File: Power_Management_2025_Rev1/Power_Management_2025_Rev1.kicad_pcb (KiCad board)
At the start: 2 copper layers, 213.1 x 179.3 mm, 100 parts, among them J1 RJ45_LED_Shielded, Q1 BSS138, Q2 IPB180N10S4-02, Q3 IPB180N10S4-02, Q4 IPB180N10S4-02, U1 Teensy4.1_DEV-16771, U10 LT1910, U11 LT1910, U12 PKE3316ZPI, U13 PKE3316ZPI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

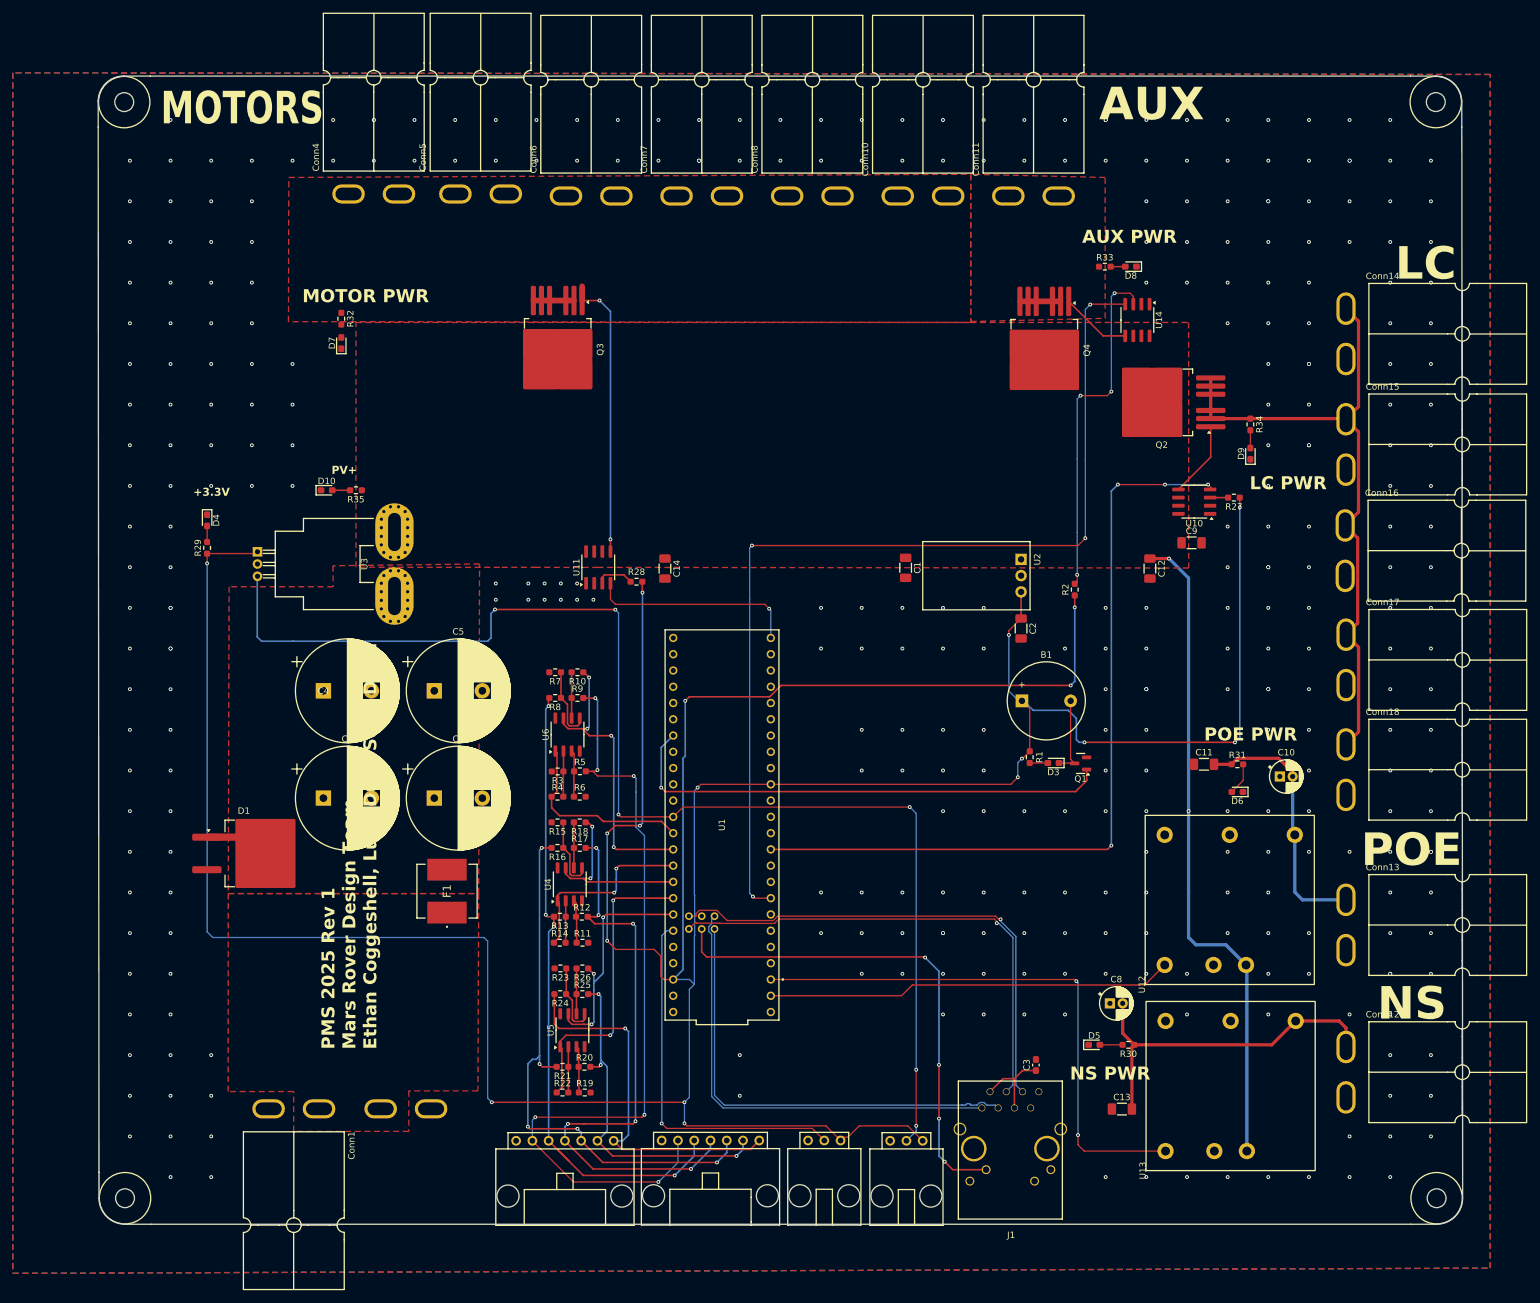
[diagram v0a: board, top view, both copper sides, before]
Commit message: Power plane, diff pair, and mil width fix`
Fixed Motor power plane, readjusted diff pair, and fixed mil width
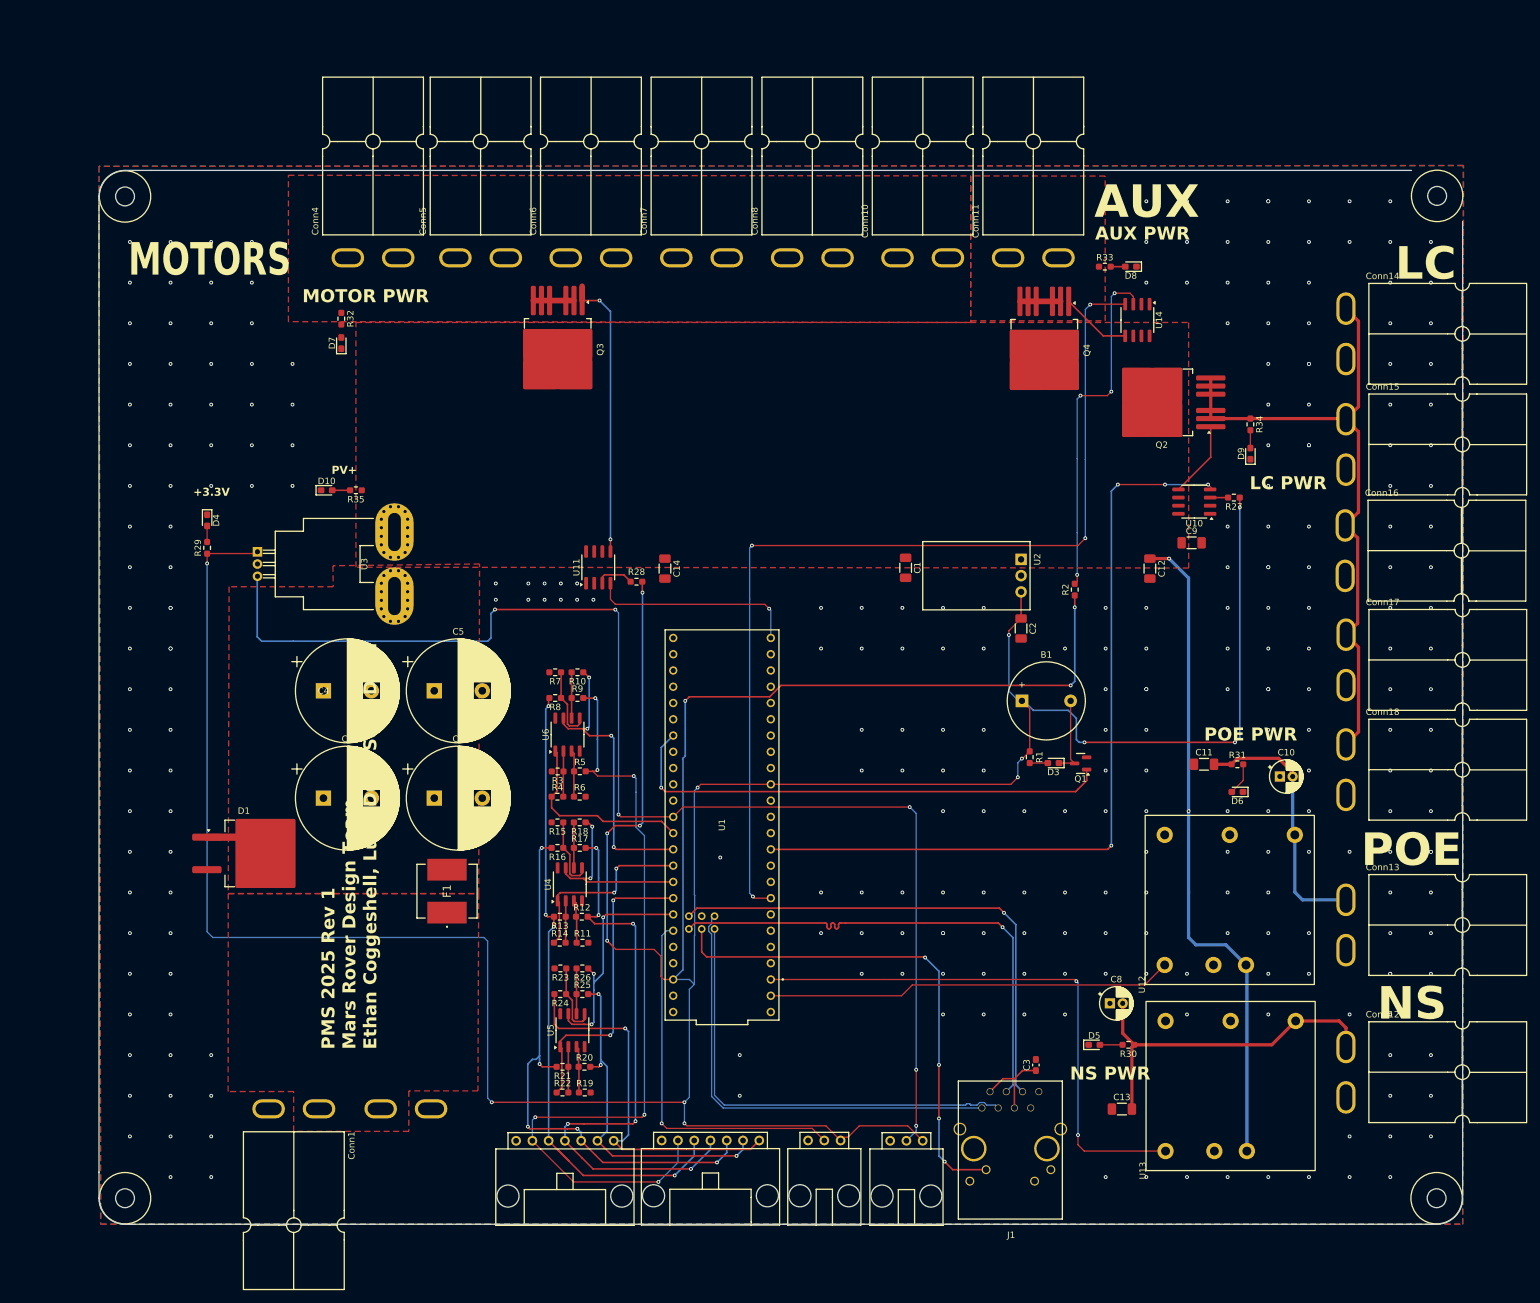
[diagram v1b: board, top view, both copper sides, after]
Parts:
- moved H3 14.7 mm to (35.0, 35.0)
- moved H1 14.7 mm to (231.9, 34.9)
- moved Conn4 9.97 mm to (74.0, 40.7)
- moved Conn5 9.97 mm to (90.8, 40.7)
- moved Conn11 9.65 mm to (177.1, 40.7)
- moved Conn6 9.65 mm to (108.0, 40.7)
- moved Conn7 9.65 mm to (125.3, 40.7)
- moved Conn8 9.65 mm to (142.6, 40.7)
- moved Conn10 9.65 mm to (159.8, 40.7)
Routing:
- net RX+: track 77.3 -> 79.1 mm
- net GND: vias 353 -> 282
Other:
- board size 213.1 x 179.3 mm -> 213 x 164.6 mm

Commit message: Fixed diff pair and rearranged Cap bank
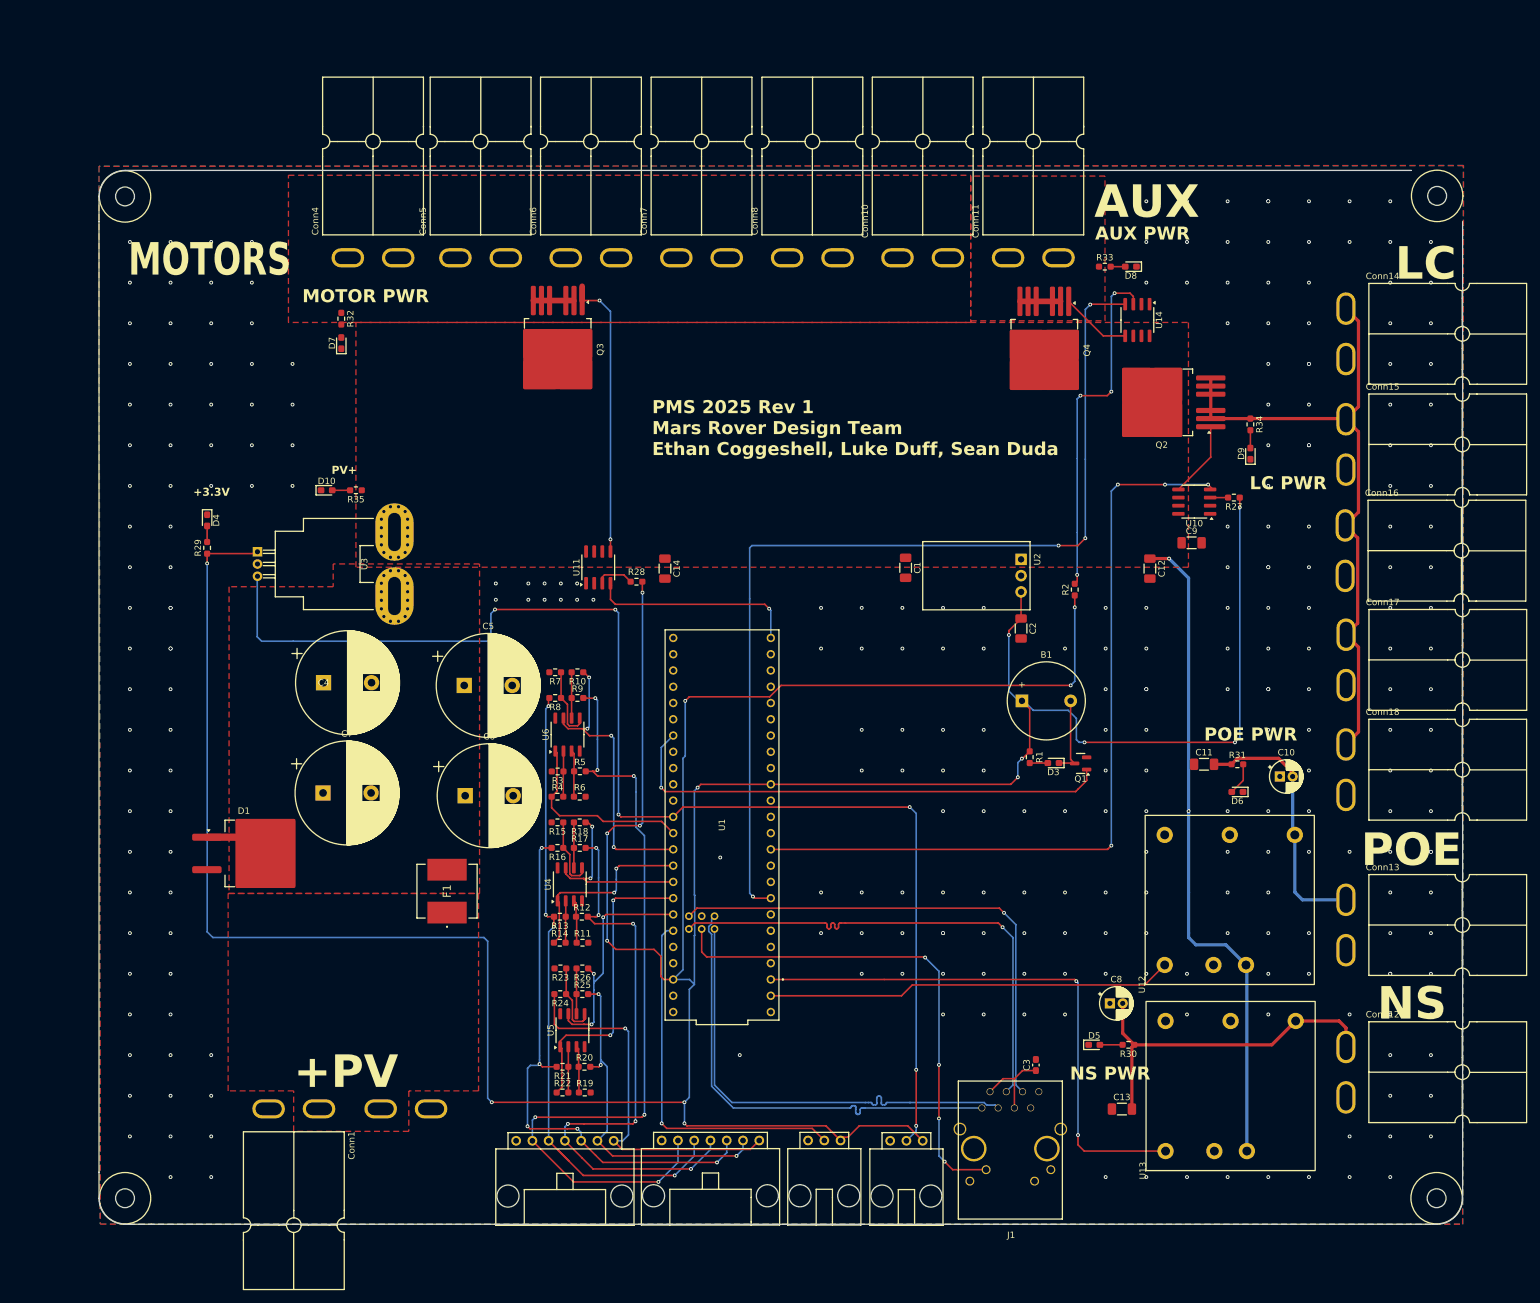
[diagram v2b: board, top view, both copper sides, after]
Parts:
- moved C6 4.84 mm to (84.1, 124.6)
- moved C5 4.75 mm to (84.0, 107.4)
- moved C4 1.27 mm to (62.0, 106.9)
- moved C7 0.81 mm to (61.9, 124.2)
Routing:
- net TX+: track 71.7 -> 72.9 mm
- net TX-: track 71.7 -> 72.8 mm
- net CELL4: track 87.1 -> 86.4 mm
- net GND: vias 282 -> 281
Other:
- board text added: "+PV"

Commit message: Retraced current sense trace, connected opamps to IP-, and made sure no traces in between resistor pads
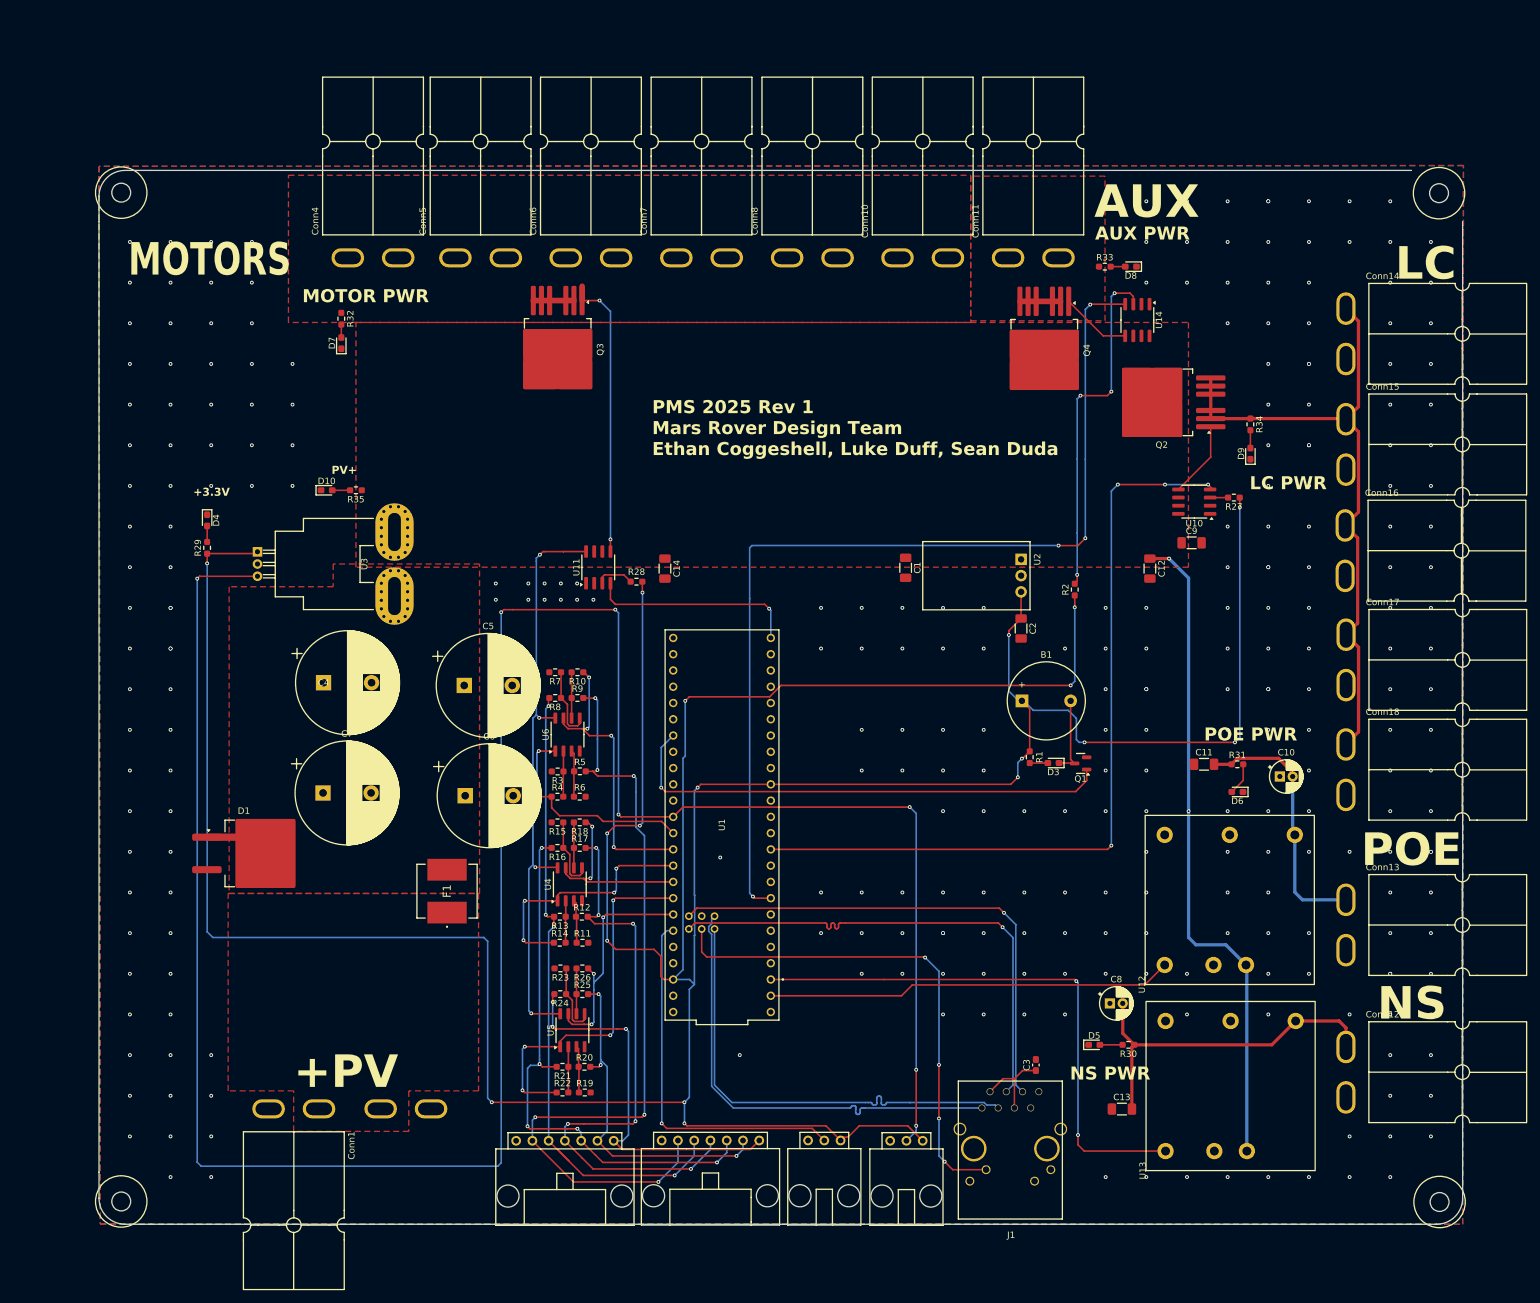
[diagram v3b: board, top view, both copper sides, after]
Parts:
- moved H3 0.83 mm to (34.4, 34.4)
- moved H4 0.78 mm to (34.4, 184.0)
- moved H2 0.75 mm to (232.3, 184.0)
- moved H1 0.52 mm to (232.2, 34.5)
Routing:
- net CURRENT_SENSE: track 201.3 -> 384.3 mm, vias 6 -> 7
- net IP-: track 103.3 -> 195.0 mm, vias 2 -> 6
- net CELL_SENSE_5: track 47.4 -> 57.8 mm, vias 2 -> 4
- net CELL_SENSE_3: track 29.9 -> 39.2 mm, vias 2 -> 4
- net CELL_SENSE_1: track 29.9 -> 34.3 mm, vias 0 -> 2
- net Net-(D7-A): track 0.00 -> 2.02 mm
- net CELL6: track 59.5 -> 60.1 mm, vias 1 -> 3
- net GND: vias 281 -> 280
